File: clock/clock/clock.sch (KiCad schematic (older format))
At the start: 18 parts

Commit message: refactor code
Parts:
- added IC?: HT16K33, HT16K33, symbol HT16K33:HT16K33
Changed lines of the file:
@@
 Wire Wire Line
 	5350 4750 5350 4650
+$Comp
+L HT16K33:HT16K33 IC?
+U 1 1 6322F161
+P 8400 4950
+F 0 "IC?" H 8400 6217 50  0000 C CNN
+F 1 "HT16K33" H 8400 6126 50  0000 C CNN
+F 2 "HT16K33" H 8400 4950 50  0001 L BNN
+F 3 "" H 8400 4950 50  0001 L BNN
+F 4 "IC-14891" H 8400 4950 50  0001 L BNN "PROD_ID"
+F 5 "HTK16K33" H 8400 4950 50  0001 L BNN "VALUE"
+	1    8400 4950
+	1    0    0    -1
+$EndComp
 $EndSCHEMATC

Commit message: switch to attiny84 and think more about control scheme
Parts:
- removed D?: LED, symbol Device:LED
- removed J?: OUT, symbol Connector:AudioJack2
- removed R?: 220, symbol Device:R
- removed RV?: R_POT, symbol Device:R_POT
- removed U?: ATmega328P-PU, Package_DIP:DIP-28_W7.62mm, symbol MCU_Microchip_ATmega:ATmega328P-PU
- added R? (x2): 10k, symbol Device:R
- added R? (x7): 1K, symbol Device:R
- added R?: 10K, symbol Device:R
- added SW?: SW_Rotary8, symbol Switch:SW_Rotary8
- added SW?: SW_Push, symbol Switch:SW_Push
- added U? (x3): HDSP-A153, Display_7Segment:HDSP-A151, symbol Display_Character:HDSP-A153
- added U?: L7805, symbol Regulator_Linear:L7805
- added U?: ATtiny84-20PU, Package_DIP:DIP-14_W7.62mm, symbol MCU_Microchip_ATtiny:ATtiny84-20PU
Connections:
- net labels added: CLOCK_OUT, KNOB, SCL, SDA, SUBDIV_OUT, SW1, SW2
- wire segments 53 -> 214
- no-connect marks 2 -> 11
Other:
- note added: "A little tight, but could connect top and bottom with 3x 6-pin headers"
- note added: "LED power draw can be high, so separate\nLED power"
- note added: "SCL/SDA pins assume Adafruit TinyWireM lib"
- moved on the sheet: C?, J?, R?, SW?, Y?

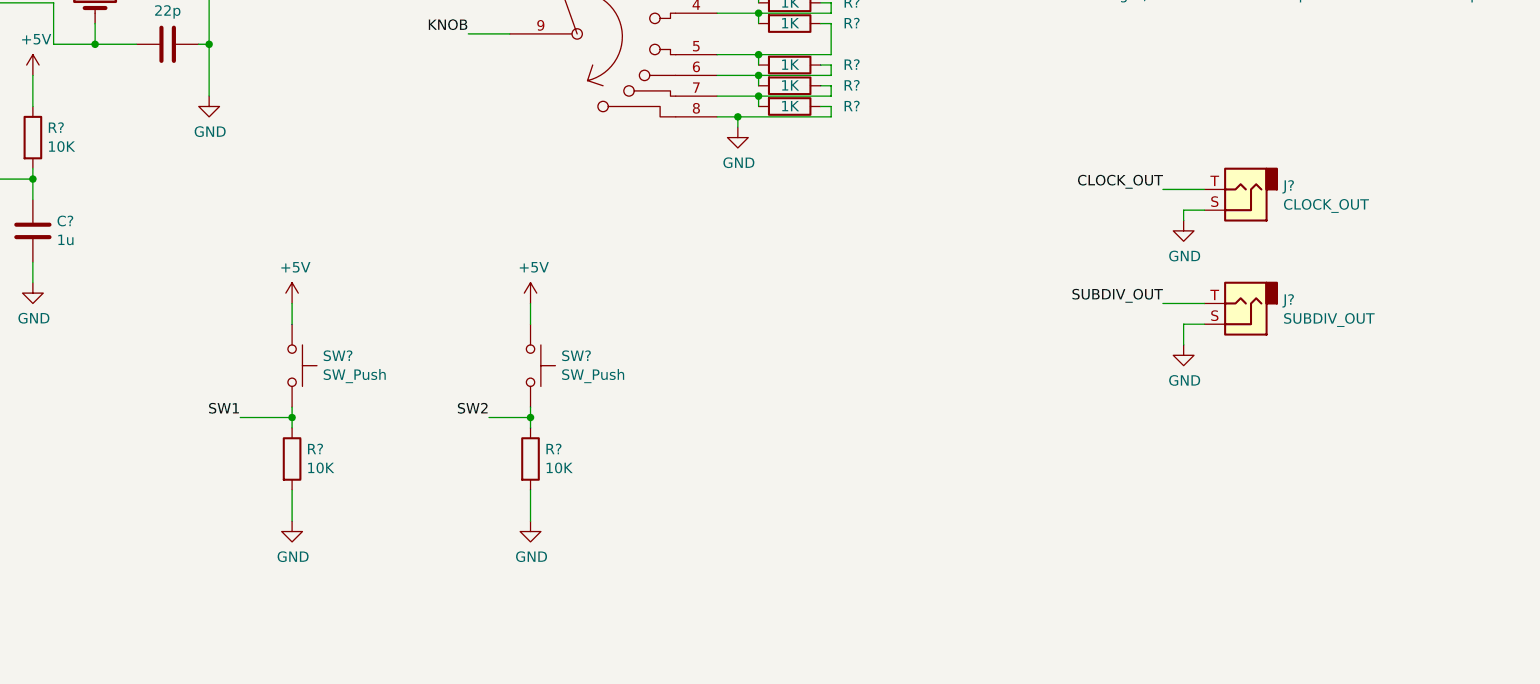
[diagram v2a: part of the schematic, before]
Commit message: move reference to blog
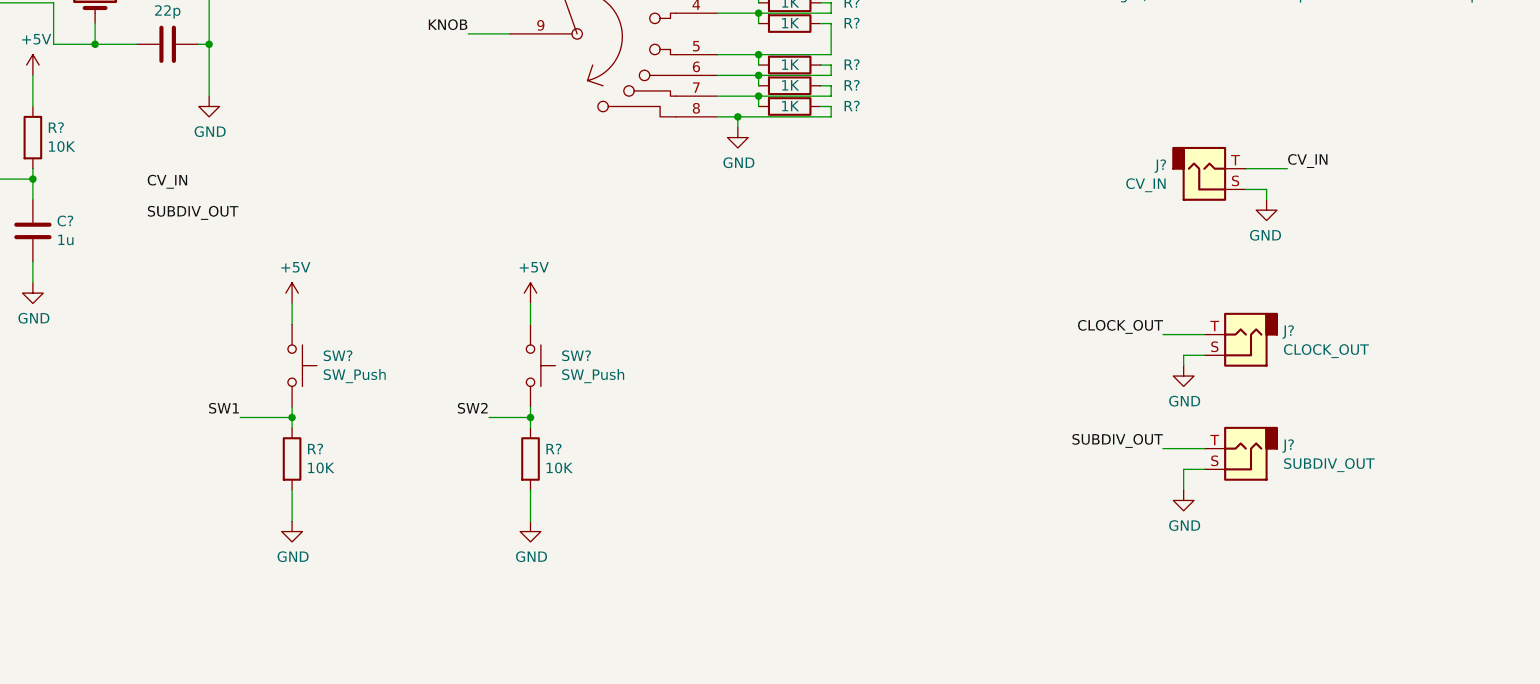
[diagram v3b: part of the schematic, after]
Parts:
- added J?: CV_IN, symbol Connector:AudioJack2
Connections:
- net labels added: CV_IN
- wire segments 214 -> 217
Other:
- moved on the sheet: J?
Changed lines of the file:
@@
 L Connector:AudioJack2 J?
 U 1 1 6321922B
-P 8700 4650
-F 0 "J?" H 8520 4633 50  0000 R CNN
-F 1 "CLOCK_OUT" H 8520 4724 50  0000 R CNN
-F 2 "" H 8700 4650 50  0001 C CNN
-F 3 "~" H 8700 4650 50  0001 C CNN
-	1    8700 4650
+P 8700 5350
+F 0 "J?" H 8520 5333 50  0000 R CNN
+F 1 "CLOCK_OUT" H 8520 5424 50  0000 R CNN
+F 2 "" H 8700 5350 50  0001 C CNN
+F 3 "~" H 8700 5350 50  0001 C CNN
+	1    8700 5350
 	-1   0    0    1
 $EndComp
@@
 L Connector:AudioJack2 J?
 U 1 1 6321A6EF
-P 8700 5200
-F 0 "J?" H 8520 5183 50  0000 R CNN
-F 1 "SUBDIV_OUT" H 8520 5274 50  0000 R CNN
-F 2 "" H 8700 5200 50  0001 C CNN
-F 3 "~" H 8700 5200 50  0001 C CNN
-	1    8700 5200
+P 8700 5900
+F 0 "J?" H 8520 5883 50  0000 R CNN
+F 1 "SUBDIV_OUT" H 8520 5974 50  0000 R CNN
+F 2 "" H 8700 5900 50  0001 C CNN
+F 3 "~" H 8700 5900 50  0001 C CNN
+	1    8700 5900
 	-1   0    0    1
 $EndComp
@@
 L power:GND #PWR?
 U 1 1 6321AD75
-P 8400 5400
-F 0 "#PWR?" H 8400 5150 50  0001 C CNN
-F 1 "GND" H 8405 5227 50  0000 C CNN
-F 2 "" H 8400 5400 50  0001 C CNN
-F 3 "" H 8400 5400 50  0001 C CNN
-	1    8400 5400
+P 8400 6100
+F 0 "#PWR?" H 8400 5850 50  0001 C CNN
+F 1 "GND" H 8405 5927 50  0000 C CNN
+F 2 "" H 8400 6100 50  0001 C CNN
+F 3 "" H 8400 6100 50  0001 C CNN
+	1    8400 6100
 	1    0    0    -1
 $EndComp
@@
 L power:GND #PWR?
 U 1 1 6321B0CD
-P 8400 4800
-F 0 "#PWR?" H 8400 4550 50  0001 C CNN
-F 1 "GND" H 8405 4627 50  0000 C CNN
-F 2 "" H 8400 4800 50  0001 C CNN
-F 3 "" H 8400 4800 50  0001 C CNN
-	1    8400 4800
-	1    0    0    -1
-$EndComp
-Wire Wire Line
-	8400 4800 8400 4750
-Wire Wire Line
-	8400 4750 8500 4750
-Wire Wire Line
-	8400 5400 8400 5300
-Wire Wire Line
-	8400 5300 8500 5300
+P 8400 5500
+F 0 "#PWR?" H 8400 5250 50  0001 C CNN
+F 1 "GND" H 8405 5327 50  0000 C CNN
+F 2 "" H 8400 5500 50  0001 C CNN
+F 3 "" H 8400 5500 50  0001 C CNN
+	1    8400 5500
+	1    0    0    -1
+$EndComp
+Wire Wire Line
+	8400 5500 8400 5450
+Wire Wire Line
+	8400 5450 8500 5450
+Wire Wire Line
+	8400 6100 8400 6000
+Wire Wire Line
+	8400 6000 8500 6000
 $Comp
 L Switch:SW_Push SW?
@@
 Wire Wire Line
 	4950 3900 5150 3900
-Text Label 8300 4650 2    50   ~ 0
+Text Label 8300 5350 2    50   ~ 0
 CLOCK_OUT
-Text Label 8300 5200 2    50   ~ 0
+Text Label 8300 5900 2    50   ~ 0
 SUBDIV_OUT
 Wire Wire Line
-	8300 5200 8500 5200
-Wire Wire Line
-	8300 4650 8500 4650
+	8300 5900 8500 5900
+Wire Wire Line
+	8300 5350 8500 5350
 $Comp
 L Switch:SW_Push SW?
@@
 Text Notes 7800 3750 0    50   ~ 0
 A little tight, but could connect top and bottom with 3x 6-pin headers
+$Comp
+L Connector:AudioJack2 J?
+U 1 1 6328406C
+P 8500 4550
+F 0 "J?" H 8320 4533 50  0000 R CNN
+F 1 "CV_IN" H 8320 4624 50  0000 R CNN
+F 2 "" H 8500 4550 50  0001 C CNN
+F 3 "~" H 8500 4550 50  0001 C CNN
+	1    8500 4550
+	1    0    0    1
+$EndComp
+$Comp
+L power:GND #PWR?
+U 1 1 63284076
+P 8800 4700
+F 0 "#PWR?" H 8800 4450 50  0001 C CNN
+F 1 "GND" H 8805 4527 50  0000 C CNN
+F 2 "" H 8800 4700 50  0001 C CNN
+F 3 "" H 8800 4700 50  0001 C CNN
+	1    8800 4700
+	-1   0    0    -1
+$EndComp
+Wire Wire Line
+	8800 4700 8800 4650
+Wire Wire Line
+	8800 4650 8700 4650
+Text Label 8900 4550 0    50   ~ 0
+CV_IN
+Wire Wire Line
+	8900 4550 8700 4550
+Text Label 3400 4650 0    50   ~ 0
+CV_IN
+Text Label 3400 4800 0    50   ~ 0
+SUBDIV_OUT
 $EndSCHEMATC

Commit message: rework clock circuit
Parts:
- removed C?: 1u, symbol Device:C
- removed IC?: HT16K33, HT16K33, symbol HT16K33:HT16K33
- removed J?: EURORACK_CONN_16, synth:EURORACK_16_IDC, symbol synth:EURORACK_CONN_16
- removed R? (x2): 10k, symbol Device:R
- removed U? (x3): HDSP-A153, Display_7Segment:HDSP-A151, symbol Display_Character:HDSP-A153
- removed U?: ATtiny84-20PU, Package_DIP:DIP-14_W7.62mm, symbol MCU_Microchip_ATtiny:ATtiny84-20PU
- added D1, D2: LED, LED_THT:LED_D3.0mm, symbol Device:LED
- added J2: EURORACK_CONN_10, synth:EURORACK_10_IDC, symbol synth:EURORACK_CONN_10
- added R2, R3: 1K, Resistor_THT:R_Axial_DIN0207_L6.3mm_D2.5mm_P2.54mm_Vertical, symbol Device:R
- added U1: ATmega328P-PU, Package_DIP:DIP-28_W7.62mm, symbol MCU_Microchip_ATmega:ATmega328P-PU
- added U3, U4, U5: SM460281N, synth:SM460281N_ARKLED_0.28mm_CC_7-segment_LED, symbol synth:SM460281N
- C1: renamed from C?; footprint (none) -> Capacitor_THT:CP_Radial_Tantal_D4.5mm_P2.50mm
- C2, C3, C4: renamed from C?; footprint (none) -> Capacitor_THT:C_Rect_L7.0mm_W3.5mm_P5.00mm
- J1: renamed from J?; footprint (none) -> Connector_PinHeader_2.54mm:PinHeader_2x03_P2.54mm_Vertical
- J3, J4, J5: renamed from J?; footprint (none) -> synth:Jack_3.5mm_QingPu_WQP-PJ398SM_Vertical_CircularHoles
- R1, R10, R11, R12, R4, R5, R6, R7, R8, R9: renamed from R?; footprint (none) -> Resistor_THT:R_Axial_DIN0207_L6.3mm_D2.5mm_P2.54mm_Vertical
- SW1, SW2: renamed from SW?; footprint (none) -> Button_Switch_THT:SW_PUSH_6mm
- SW3: renamed from SW?; footprint (none) -> synth:RM100772BCB
- U2: renamed from U?; footprint (none) -> Package_TO_SOT_THT:TO-220-3_Vertical
- Y1: renamed from Y?; footprint (none) -> Crystal:Crystal_HC52-8mm_Vertical
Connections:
- net labels added: LED0, LED1, LED2, LED3, LED4, LED5, LED6, LED_A, LED_B, LED_C1, LED_C2, LED_C3
- net labels removed: SCL, SDA
- wire segments 217 -> 203
- no-connect marks 11 -> 1
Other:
- note removed: "LED power draw can be high, so separate\nLED power"
- note removed: "SCL/SDA pins assume Adafruit TinyWireM lib"
- moved on the sheet: C1, C2, C3, C4, R1, U2, Y1

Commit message: proof-of-concept LED driver
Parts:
- added J10, J11, J12, J13: Conn_01x05_Male, Connector_PinHeader_2.54mm:PinHeader_1x05_P2.54mm_Vertical, symbol Connector:Conn_01x05_Male
- added J6, J7, J8, J9: Conn_01x05_Female, Connector_PinSocket_2.54mm:PinSocket_1x05_P2.54mm_Vertical, symbol Connector:Conn_01x05_Female
- added R13, R14, R15: 1K, Resistor_THT:R_Axial_DIN0207_L6.3mm_D2.5mm_P2.54mm_Vertical, symbol Device:R
- R10, R11, R12, R6, R7, R8, R9: value 1K -> 10K
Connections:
- net +5V: now also J8.4 (Pin_4); no longer D1.2 (A), D2.2 (A), R6.2, SW1.1, SW2.1, SW3.1
- net CLOCK_OUT: now also J10.1 (Pin_1); no longer U1.16 (PB2)
- net CV_IN: now also J10.3 (Pin_3); no longer U1.24 (PC1)
- net GND: now also J8.5 (Pin_5); no longer J3.S, J4.S, J5.S, R12.1, SW3.8
- net KNOB: now also J13.1 (Pin_1); no longer U1.23 (PC0)
- net LED0: now also U4.4 (E), J10.5 (Pin_5); no longer U1.2 (PD0), U4.3 (G)
- net LED1: now also J11.3 (Pin_3); no longer U1.3 (PD1)
- net LED2: now also U4.3 (G), J11.1 (Pin_1); no longer U1.4 (PD2), U4.4 (E)
- net LED3: now also U4.8 (A), J11.4 (Pin_4); no longer U1.5 (PD3), U4.5 (D)
- net LED4: now also U4.7 (B), J12.1 (Pin_1); no longer U1.6 (PD4), U4.6 (C)
- net LED5: now also U4.6 (C), J12.2 (Pin_2); no longer U1.11 (PD5), U4.7 (B)
- net LED6: now also U4.5 (D), J12.3 (Pin_3); no longer U1.12 (PD6), U4.8 (A)
- net LED_A: now also J13.3 (Pin_3); no longer U1.28 (PC5)
- net LED_B: now also J13.4 (Pin_4); no longer U1.13 (PD7)
- net LED_C1: now also J10.4 (Pin_4); no longer U1.25 (PC2)
- net LED_C2: now also J11.2 (Pin_2); no longer U1.26 (PC3)
- net LED_C3: now also J11.5 (Pin_5); no longer U1.27 (PC4)
- net SW1: now also J13.2 (Pin_2); no longer U1.14 (PB0)
- net SW2: now also J13.5 (Pin_5); no longer U1.15 (PB1)
- net at R9.1, SW3.5: now also R10.1; no longer R10.2
- net at R12.2, SW3.7: now also R11.2; no longer R11.1
- net MOSI renamed B_SUBDIV_OUT
- net B_SUBDIV_OUT: now also J6.2 (Pin_2); no longer J5.T
- new net: R13.2, U1.25 (PC2)
- new net: R14.2, U1.26 (PC3)
- new net: R15.2, U1.27 (PC4)
- new net: R10.2, R11.1, SW3.6
- new net AGND: J12.5 (Pin_5), J3.S, J4.S, J5.S, R12.1, SW3.8
- new net AVCC: D1.2 (A), D2.2 (A), J12.4 (Pin_4), R6.2, SW1.1, SW2.1, SW3.1
- new net B_CLOCK_OUT: J6.1 (Pin_1), U1.16 (PB2)
- new net B_CV_IN: J6.3 (Pin_3), U1.24 (PC1)
- new net B_KNOB: J9.1 (Pin_1), U1.23 (PC0)
- new net B_LED0: J6.4 (Pin_4), U1.2 (PD0)
- new net B_LED1: J6.5 (Pin_5), U1.3 (PD1)
- new net B_LED2: J7.1 (Pin_1), U1.4 (PD2)
- new net B_LED3: J7.2 (Pin_2), U1.5 (PD3)
- new net B_LED4: J7.3 (Pin_3), U1.6 (PD4)
- new net B_LED5: J7.4 (Pin_4), U1.11 (PD5)
- new net B_LED6: J7.5 (Pin_5), U1.12 (PD6)
- new net B_LED_A: J9.3 (Pin_3), U1.28 (PC5)
- new net B_LED_B: J9.4 (Pin_4), U1.13 (PD7)
- new net B_LED_C1: J8.1 (Pin_1), R13.1
- new net B_LED_C2: J8.2 (Pin_2), R14.1
- new net B_LED_C3: J8.3 (Pin_3), R15.1
- new net B_SW1: J9.2 (Pin_2), U1.14 (PB0)
- new net B_SW2: J9.5 (Pin_5), U1.15 (PB1)
- new net SUBDIV_OUT: J10.2 (Pin_2), J5.T
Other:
- note removed: "A little tight, but could connect top and bottom with 3x 6-pin headers"
- moved on the sheet: J3, J4, J5
